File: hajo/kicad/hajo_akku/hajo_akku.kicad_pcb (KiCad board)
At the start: 2 copper layers, 68.6 x 71.1 mm, 18 parts, among them J1 Seetalk NG, J2 Batteries, J4 Device type, U1 MCP2562, U2 LF50CV

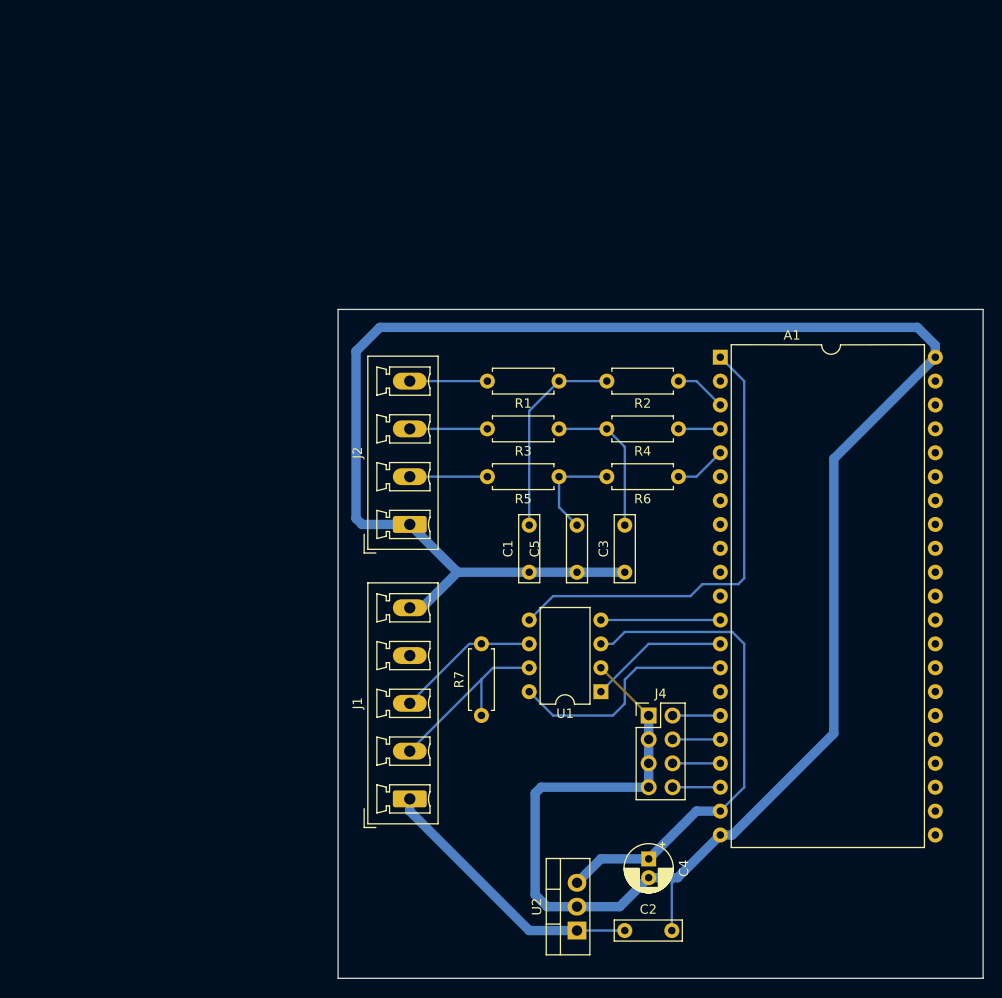
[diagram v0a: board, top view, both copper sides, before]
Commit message: kicad fix schematic
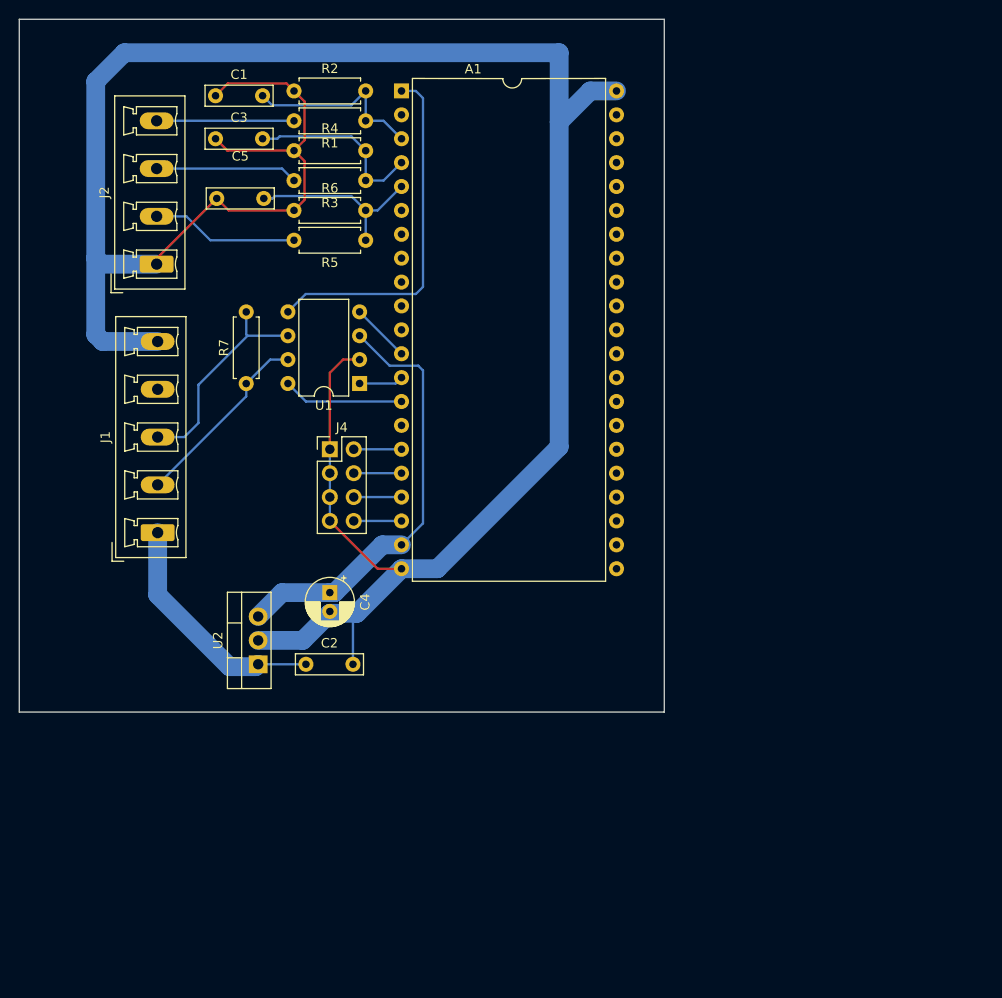
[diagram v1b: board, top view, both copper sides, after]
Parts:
- moved C3 63.4 mm to (32.7, 25.0), turned to 0 degrees
- moved C1 60.7 mm to (32.7, 20.5), turned to 0 degrees
- moved C5 55.2 mm to (32.8, 31.4), turned to 0 degrees
- moved R2 51.2 mm to (41.0, 19.9), turned to 0 degrees
- moved R4 50.5 mm to (41.0, 26.3), turned to 0 degrees
- moved R6 49.7 mm to (41.0, 32.6), turned to 0 degrees
- moved A1 44.2 mm to (52.5, 19.9)
- moved U2 44.2 mm to (37.2, 80.9)
- moved C2 44.2 mm to (42.3, 80.9)
- moved C4 44.2 mm to (44.8, 73.3)
- moved J4 44.2 mm to (44.8, 58.0)
- moved R7 43.2 mm to (36.0, 51.1)
- moved U1 41.6 mm to (48.0, 51.1)
- moved J1 39.0 mm to (26.5, 66.9)
- moved J2 38.6 mm to (26.4, 38.4)
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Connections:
- C1 pad 2: Net-(C1-Pad2) -> /ADC1
- C3 pad 2: Net-(C3-Pad2) -> /ADC2
- C5 pad 2: Net-(C5-Pad2) -> /ADC3
- R1 pad 1: Net-(C1-Pad2) -> /ADC1
- R2 pad 1: /ADC1 -> GND
- R2 pad 2: Net-(C1-Pad2) -> /ADC1
- R3 pad 1: Net-(C3-Pad2) -> /ADC2
- R4 pad 1: /ADC2 -> GND
- R4 pad 2: Net-(C3-Pad2) -> /ADC2
- R5 pad 1: Net-(C5-Pad2) -> /ADC3
- R6 pad 1: /ADC3 -> GND
- R6 pad 2: Net-(C5-Pad2) -> /ADC3
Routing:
- net Net-(C1-Pad2): track 21.7 -> 0.00 mm
- net GND: track 248.3 -> 266.8 mm
- net Net-(C3-Pad2): track 16.1 -> 0.00 mm
- net /ADC2: track 4.45 -> 19.3 mm
- net /ADC1: track 5.50 -> 19.8 mm
- net /ADC3: track 5.50 -> 19.6 mm
- net /STBY: track 25.0 -> 12.9 mm
- net +3.3V: track 49.2 -> 38.1 mm
- net Net-(C5-Pad2): track 11.0 -> 0.00 mm
- net /TXD: track 14.8 -> 4.71 mm
- net /CANL: track 15.3 -> 23.3 mm
- net Net-(J2-Pin_2): track 8.25 -> 15.7 mm
- net +5V: track 53.5 -> 46.2 mm
- net Net-(J2-Pin_3): track 8.25 -> 15.1 mm
- net /RXD: track 12.7 -> 6.30 mm
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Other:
- board size 68.6 x 71.1 mm -> 68.6 x 73.7 mm

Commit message: final pcb
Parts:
- removed J4: Device type, Connector_PinHeader_2.54mm:PinHeader_2x04_P2.54mm_Vertical
- added H1: MountingHole, MountingHole:MountingHole_3.2mm_M3, F.Cu at (76.9, 21.4)
- added H2: MountingHole, MountingHole:MountingHole_3.2mm_M3, F.Cu at (18.6, 93.9)
- added H3: MountingHole, MountingHole:MountingHole_3.2mm_M3, F.Cu at (18.6, 21.6)
- added H4: MountingHole, MountingHole:MountingHole_3.2mm_M3, F.Cu at (76.9, 93.9)
- added J3: Terminator, Connector_PinHeader_2.54mm:PinHeader_2x02_P2.54mm_Vertical, F.Cu at (38.6, 72.4)
- U2: footprint Package_TO_SOT_THT:TO-220-3_Vertical -> Package_TO_SOT_THT:TO-220-3_Horizontal_TabDown
- moved U1 24.5 mm to (50.3, 75.5)
- moved C4 17.1 mm to (52.6, 88.5)
- moved U2 17.1 mm to (45.0, 96.1)
- moved C2 17.1 mm to (50.1, 96.1)
- moved R7 12.9 mm to (34.1, 63.8), turned to 0 degrees
- moved J1 11.2 mm to (28.2, 78.0)
- moved J2 11.2 mm to (28.1, 49.4)
- moved R4 11.2 mm to (42.7, 37.4)
- moved R5 11.2 mm to (50.3, 46.9)
- moved A1 11.2 mm to (54.1, 31.0)
- moved C1 11.2 mm to (34.4, 31.5)
- moved C3 11.2 mm to (34.4, 36.1)
- moved C5 11.2 mm to (34.5, 42.5)
- moved R1 11.2 mm to (50.3, 34.2)
- moved R2 11.2 mm to (42.7, 31.0)
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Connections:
- A1 pad 12: /RXD -> GND
- A1 pad 13: /TXD -> unconnected-(A1-GPIO11/ADC2_0-Pad13)
- A1 pad 14: /STBY -> unconnected-(A1-GPIO12/ADC2_1-Pad14)
- A1 pad 16: Net-(A1-GPIO14/ADC2_3) -> unconnected-(A1-GPIO14/ADC2_3-Pad16)
- A1 pad 17: Net-(A1-GPIO15/ADC2_4/U0RTS) -> /RXD
- A1 pad 18: Net-(A1-GPIO16/ADC2_5/U0CTS) -> /TXD
- A1 pad 19: Net-(A1-GPIO17/ADC2_6/U1TXD) -> /STBY
- J1 pad 4: unconnected-(J1-Pin_4-Pad4) -> GND
- R7 pad 1: /CANH -> Net-(J3-Pin_2)
- R7 pad 2: /CANL -> Net-(J3-Pin_4)
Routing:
- net GND: track 266.8 -> 299.8 mm
- net +5V: track 46.2 -> 34.2 mm
- net Net-(J3-Pin_2): track 0.00 -> 9.48 mm
- net Net-(J3-Pin_4): track 0.00 -> 8.41 mm
- net /CANL: track 23.3 -> 15.5 mm
- net +12V: track 25.6 -> 31.9 mm
- net +3.3V: track 38.1 -> 44.0 mm
- net Net-(A1-GPIO17/ADC2_6/U1TXD): track 5.08 -> 0.00 mm
- net Net-(A1-GPIO16/ADC2_5/U0CTS): track 5.08 -> 0.00 mm
- net Net-(A1-GPIO15/ADC2_4/U0RTS): track 5.08 -> 0.00 mm
- net Net-(A1-GPIO14/ADC2_3): track 5.08 -> 0.00 mm
- net /CANH: track 20.2 -> 16.3 mm
- net /RXD: track 6.30 -> 5.40 mm
- net /STBY: track 12.9 -> 12.0 mm
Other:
- board size 68.6 x 73.7 mm -> 69.2 x 89.5 mm
- board text added: "12V"
- board text added: "ADC1"
- board text added: "ADC2"
- board text added: "ADC3"
- board text added: "Batteries"
- board text added: "CANH"
- board text added: "CANL"
- board text added: "GND"
- board text added: "SeaTalk NG"
- board text added: "Shield"
- board text added: "Terminator"

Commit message: fix akku
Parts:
- U1: footprint Package_DIP:DIP-8_W7.62mm -> Package_DIP:DIP-8_W7.62mm_Socket
- moved C1 0.38 mm to (34.4, 31.2)
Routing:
- net GND: track 299.8 -> 308.5 mm
